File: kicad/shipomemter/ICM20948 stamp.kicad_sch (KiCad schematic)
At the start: 8 parts, among them U101 ICM-20948, U102 TXS0108EPW

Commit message: Pulled in ICM20948
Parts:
- added G1: KwanSystems, KwanSystems:KWAN_CIRCLE, symbol KwanSystems:KwanSystems
- added G2: Designed with, KwanSystems:Symbol_KiCAD-Logo_CopperAndSilkScreenTop_small, symbol KwanSystems:DesignedWithKicad
- added G3: OSHW, KwanSystems:OSHW-Symbol_4x3.6mm_SolderMask, symbol KwanSystems:OSHW
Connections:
- net INT1_3V3: now also J101.8 (INT1); no longer J101.9 (INT1)
- net MISO_3V3: now also J101.9 (AD0); no longer J101.8 (AD0)

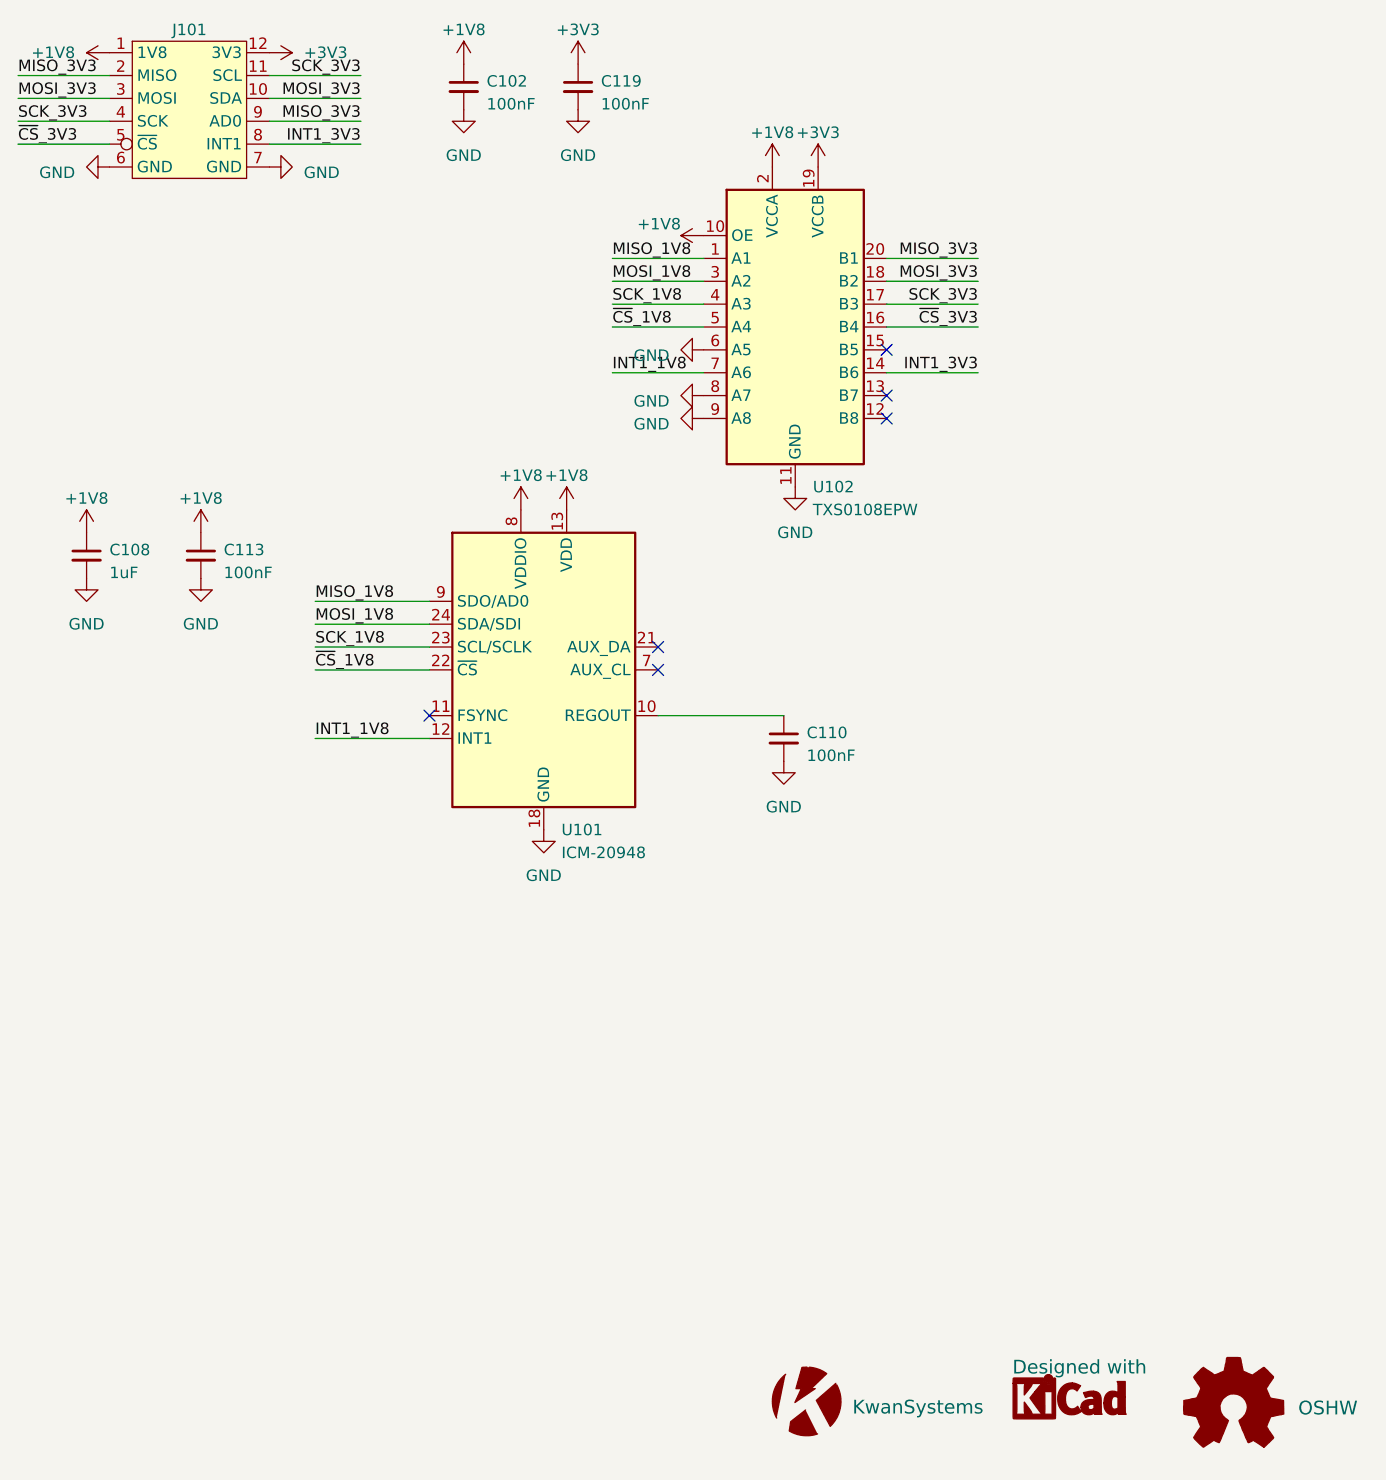
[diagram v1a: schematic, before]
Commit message: As ordered on 03 Apr 2023. Some but not all numbers-on-hand have been updated.
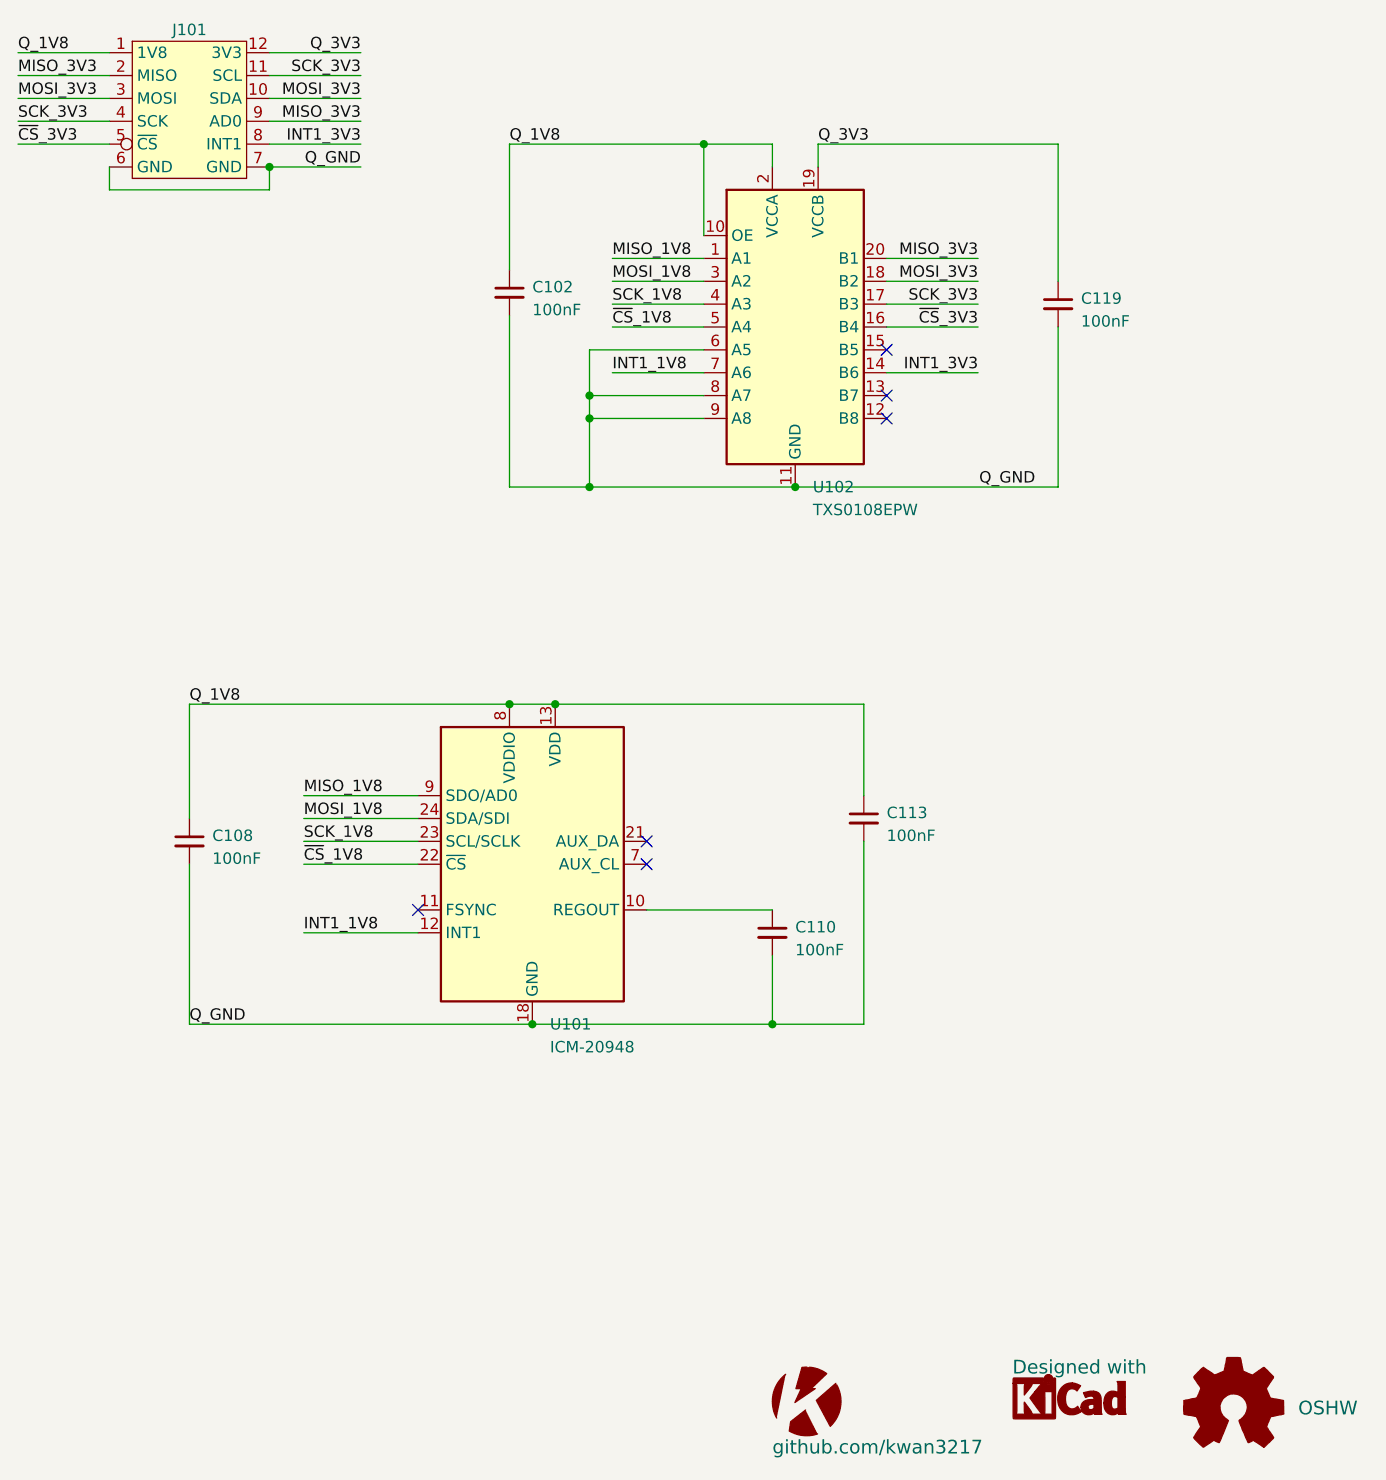
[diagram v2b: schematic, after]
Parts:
- C102, C113, C119: Digikey (none) -> 399-C0603C104M5RAC7867CT-ND; Mouser (none) -> 80-C0603C104K4P; Number in cart (none) -> 10; Number on hand (none) -> 0
- C108: value 1uF -> 100nF; Digikey (none) -> 399-C0603C104M5RAC7867CT-ND; Mouser (none) -> 80-C0603C104K4P; Number in cart (none) -> 10; Number on hand (none) -> 0
- C110: Digikey (none) -> 399-C0603C104M5RAC7867CT-ND; Mouser (none) -> 80-C0603C104K4P; Number in cart (none) -> 10; Number on hand (none) -> 0; Purpose (none) -> IMU Regulator Output
- G1: value KwanSystems -> github.com/kwan3217
- U101: Mouser (none) -> 410-ICM-20948; Number in cart (none) -> 1; Number on hand (none) -> 0
- U102: Number on hand (none) -> 9
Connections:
- net +1V8 renamed Q_1V8
- net +3V3 renamed Q_3V3
- net GND renamed Q_GND
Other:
- moved on the sheet: C102, C108, C110, C113, C119, U101

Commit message: Updated number on hand, and added more Digikey/Mouser/Mfg numbers
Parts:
- C102, C108, C110, C113, C119: Number in cart 10 -> (none); Number on hand 0 -> 10+10; Part Number (none) -> C0603C104M5RAC
- U101: Digikey (none) -> 1428-1123-1-ND; Number in cart 1 -> (none); Number on hand 0 -> 1; Part Number (none) -> ICM-20948
- U102: Digikey (none) -> 296-23011-1-ND; Mouser (none) -> 595-TXS0108EPWR; Part Number (none) -> TXS0108EPWR
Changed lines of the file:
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@@
       (effects (font (size 1.27 1.27)) hide)
     )
-    (property "Number on hand" "0" (at 113.03 110.49 0)
+    (property "Number on hand" "10+10" (at 113.03 110.49 0)
       (effects (font (size 1.27 1.27)) hide)
     )
@@
       (effects (font (size 1.27 1.27)) hide)
     )
-    (property "Number in cart" "10" (at 113.03 110.49 0)
+    (property "Number in cart" "" (at 113.03 110.49 0)
+      (effects (font (size 1.27 1.27)) hide)
+    )
+    (property "Part Number" "C0603C104M5RAC" (at 113.03 110.49 0)
       (effects (font (size 1.27 1.27)) hide)
     )
@@
       (effects (font (size 1.27 1.27)) hide)
     )
-    (property "Number on hand" "0" (at 177.8 120.65 0)
+    (property "Number on hand" "10+10" (at 177.8 120.65 0)
       (effects (font (size 1.27 1.27)) hide)
     )
@@
       (effects (font (size 1.27 1.27)) hide)
     )
-    (property "Number in cart" "10" (at 177.8 120.65 0)
+    (property "Number in cart" "" (at 177.8 120.65 0)
+      (effects (font (size 1.27 1.27)) hide)
+    )
+    (property "Part Number" "C0603C104M5RAC" (at 177.8 120.65 0)
       (effects (font (size 1.27 1.27)) hide)
     )
@@
       (effects (font (size 1.27 1.27)) hide)
     )
-    (property "Number in cart" "1" (at 151.13 113.03 0)
-      (effects (font (size 1.27 1.27)) hide)
-    )
-    (property "Number on hand" "0" (at 151.13 113.03 0)
+    (property "Number in cart" "" (at 151.13 113.03 0)
+      (effects (font (size 1.27 1.27)) hide)
+    )
+    (property "Number on hand" "1" (at 151.13 113.03 0)
+      (effects (font (size 1.27 1.27)) hide)
+    )
+    (property "Digikey" "1428-1123-1-ND" (at 151.13 113.03 0)
+      (effects (font (size 1.27 1.27)) hide)
+    )
+    (property "Part Number" "ICM-20948" (at 151.13 113.03 0)
       (effects (font (size 1.27 1.27)) hide)
     )
@@
       (effects (font (size 1.27 1.27)) hide)
     )
-    (property "Number on hand" "0" (at 148.59 49.53 0)
+    (property "Number on hand" "10+10" (at 148.59 49.53 0)
       (effects (font (size 1.27 1.27)) hide)
     )
@@
       (effects (font (size 1.27 1.27)) hide)
     )
-    (property "Number in cart" "10" (at 148.59 49.53 0)
+    (property "Number in cart" "" (at 148.59 49.53 0)
+      (effects (font (size 1.27 1.27)) hide)
+    )
+    (property "Part Number" "C0603C104M5RAC" (at 148.59 49.53 0)
       (effects (font (size 1.27 1.27)) hide)
     )
@@
     )
     (property "Number on hand" "9" (at 180.34 53.34 0)
+      (effects (font (size 1.27 1.27)) hide)
+    )
+    (property "Digikey" "296-23011-1-ND" (at 180.34 53.34 0)
+      (effects (font (size 1.27 1.27)) hide)
+    )
+    (property "Mouser" "595-TXS0108EPWR" (at 180.34 53.34 0)
+      (effects (font (size 1.27 1.27)) hide)
+    )
+    (property "Part Number" "TXS0108EPWR" (at 180.34 53.34 0)
       (effects (font (size 1.27 1.27)) hide)
     )
@@
       (effects (font (size 1.27 1.27)) hide)
     )
-    (property "Number on hand" "0" (at 187.96 107.95 0)
+    (property "Number on hand" "10+10" (at 187.96 107.95 0)
       (effects (font (size 1.27 1.27)) hide)
     )
@@
       (effects (font (size 1.27 1.27)) hide)
     )
-    (property "Number in cart" "10" (at 187.96 107.95 0)
+    (property "Number in cart" "" (at 187.96 107.95 0)
+      (effects (font (size 1.27 1.27)) hide)
+    )
+    (property "Part Number" "C0603C104M5RAC" (at 187.96 107.95 0)
       (effects (font (size 1.27 1.27)) hide)
     )
@@
       (effects (font (size 1.27 1.27)) hide)
     )
-    (property "Number on hand" "0" (at 209.55 50.8 0)
+    (property "Number on hand" "10+10" (at 209.55 50.8 0)
       (effects (font (size 1.27 1.27)) hide)
     )
@@
       (effects (font (size 1.27 1.27)) hide)
     )
-    (property "Number in cart" "10" (at 209.55 50.8 0)
-      (effects (font (size 1.27 1.27)) hide)
-    )
+    (property "Number in cart" "" (at 209.55 50.8 0)
+      (effects (font (size 1.27 1.27)) hide)
+    )
+    (property "Part Number" "C0603C104M5RAC" (at 209.55 50.8 0)
+      (effects (font (size 1.27 1.27)) hide)
+    )

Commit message: Updated stuff that was needed to make Shipometer 23.04 case
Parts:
- C102, C108, C110, C113, C119: Number on hand 10+10 -> 15
- U101: Number in cart (none) -> 1; Number on hand 1 -> 0
- U102: Number on hand 9 -> 8
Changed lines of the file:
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@@
       (effects (font (size 1.27 1.27)) hide)
     )
-    (property "Number on hand" "10+10" (at 113.03 110.49 0)
+    (property "Number on hand" "15" (at 113.03 110.49 0)
       (effects (font (size 1.27 1.27)) hide)
     )
@@
       (effects (font (size 1.27 1.27)) hide)
     )
-    (property "Number on hand" "10+10" (at 177.8 120.65 0)
+    (property "Number on hand" "15" (at 177.8 120.65 0)
       (effects (font (size 1.27 1.27)) hide)
     )
@@
       (effects (font (size 1.27 1.27)) hide)
     )
-    (property "Number in cart" "" (at 151.13 113.03 0)
-      (effects (font (size 1.27 1.27)) hide)
-    )
-    (property "Number on hand" "1" (at 151.13 113.03 0)
+    (property "Number in cart" "1" (at 151.13 113.03 0)
+      (effects (font (size 1.27 1.27)) hide)
+    )
+    (property "Number on hand" "0" (at 151.13 113.03 0)
       (effects (font (size 1.27 1.27)) hide)
     )
@@
       (effects (font (size 1.27 1.27)) hide)
     )
-    (property "Number on hand" "10+10" (at 148.59 49.53 0)
+    (property "Number on hand" "15" (at 148.59 49.53 0)
       (effects (font (size 1.27 1.27)) hide)
     )
@@
       (effects (font (size 1.27 1.27)) hide)
     )
-    (property "Number on hand" "9" (at 180.34 53.34 0)
+    (property "Number on hand" "8" (at 180.34 53.34 0)
       (effects (font (size 1.27 1.27)) hide)
     )
@@
       (effects (font (size 1.27 1.27)) hide)
     )
-    (property "Number on hand" "10+10" (at 187.96 107.95 0)
+    (property "Number on hand" "15" (at 187.96 107.95 0)
       (effects (font (size 1.27 1.27)) hide)
     )
@@
       (effects (font (size 1.27 1.27)) hide)
     )
-    (property "Number on hand" "10+10" (at 209.55 50.8 0)
-      (effects (font (size 1.27 1.27)) hide)
-    )
+    (property "Number on hand" "15" (at 209.55 50.8 0)
+      (effects (font (size 1.27 1.27)) hide)
+    )
